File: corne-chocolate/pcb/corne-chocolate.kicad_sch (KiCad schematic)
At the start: 19 parts, among them J2 nice!view, J3 Battery, J4 Battery, SW21 1.5U, SW22 SW_PUSH, SW23 SW_SPDT, U1 ProMicro

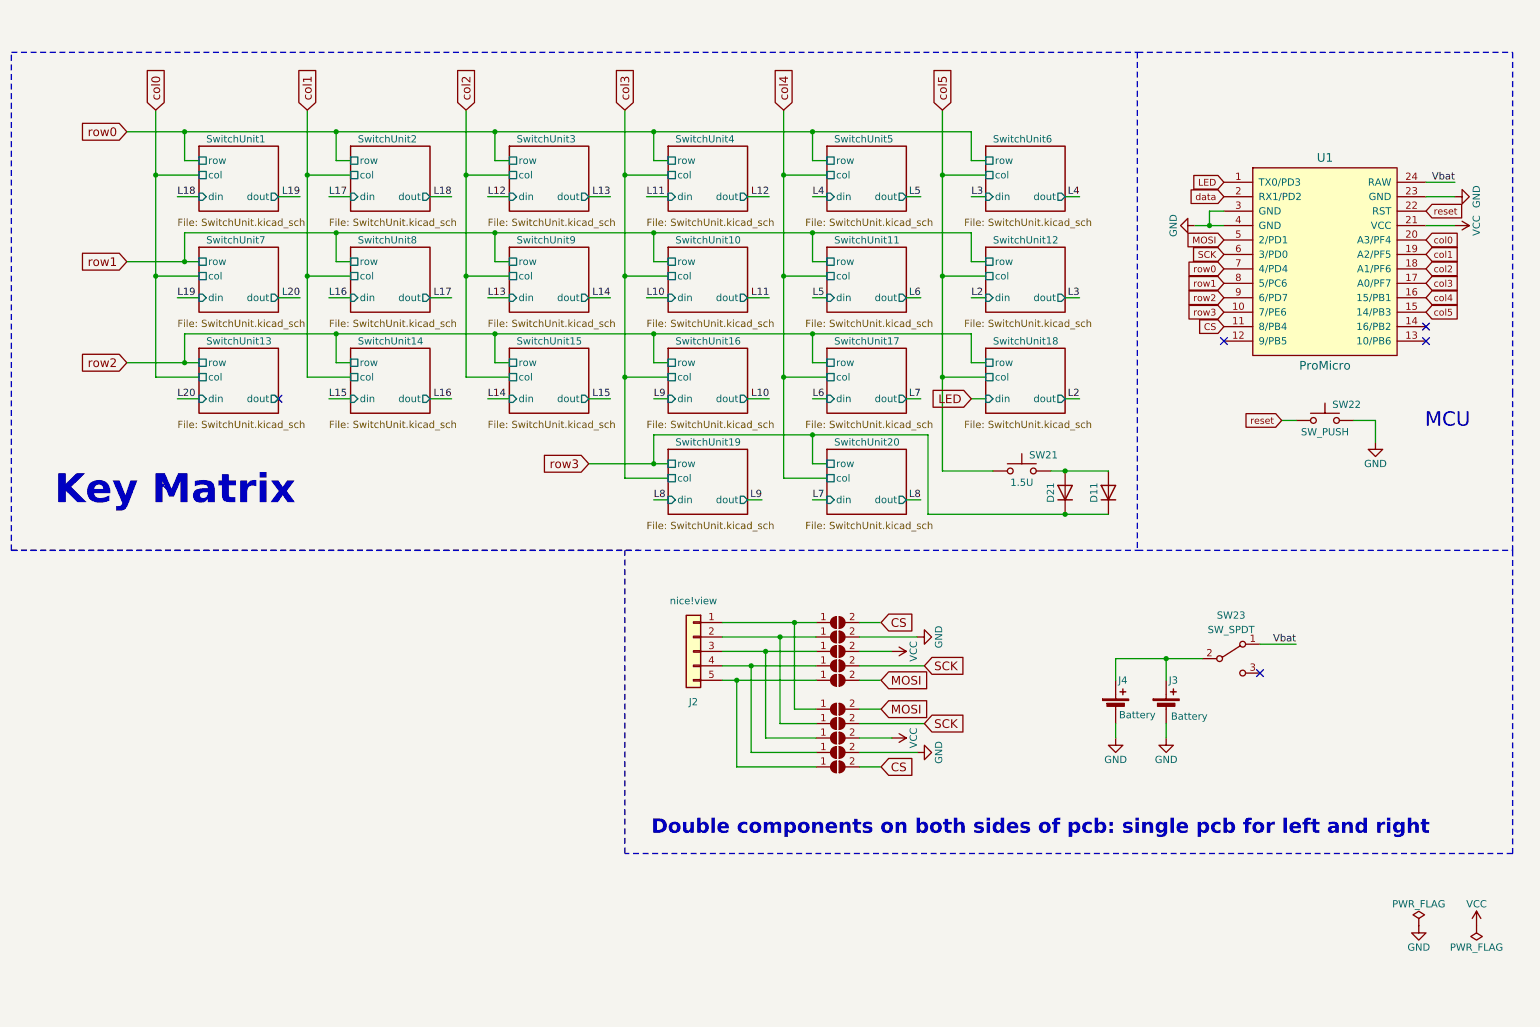
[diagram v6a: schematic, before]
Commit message: pcb remove per-switch LEDs
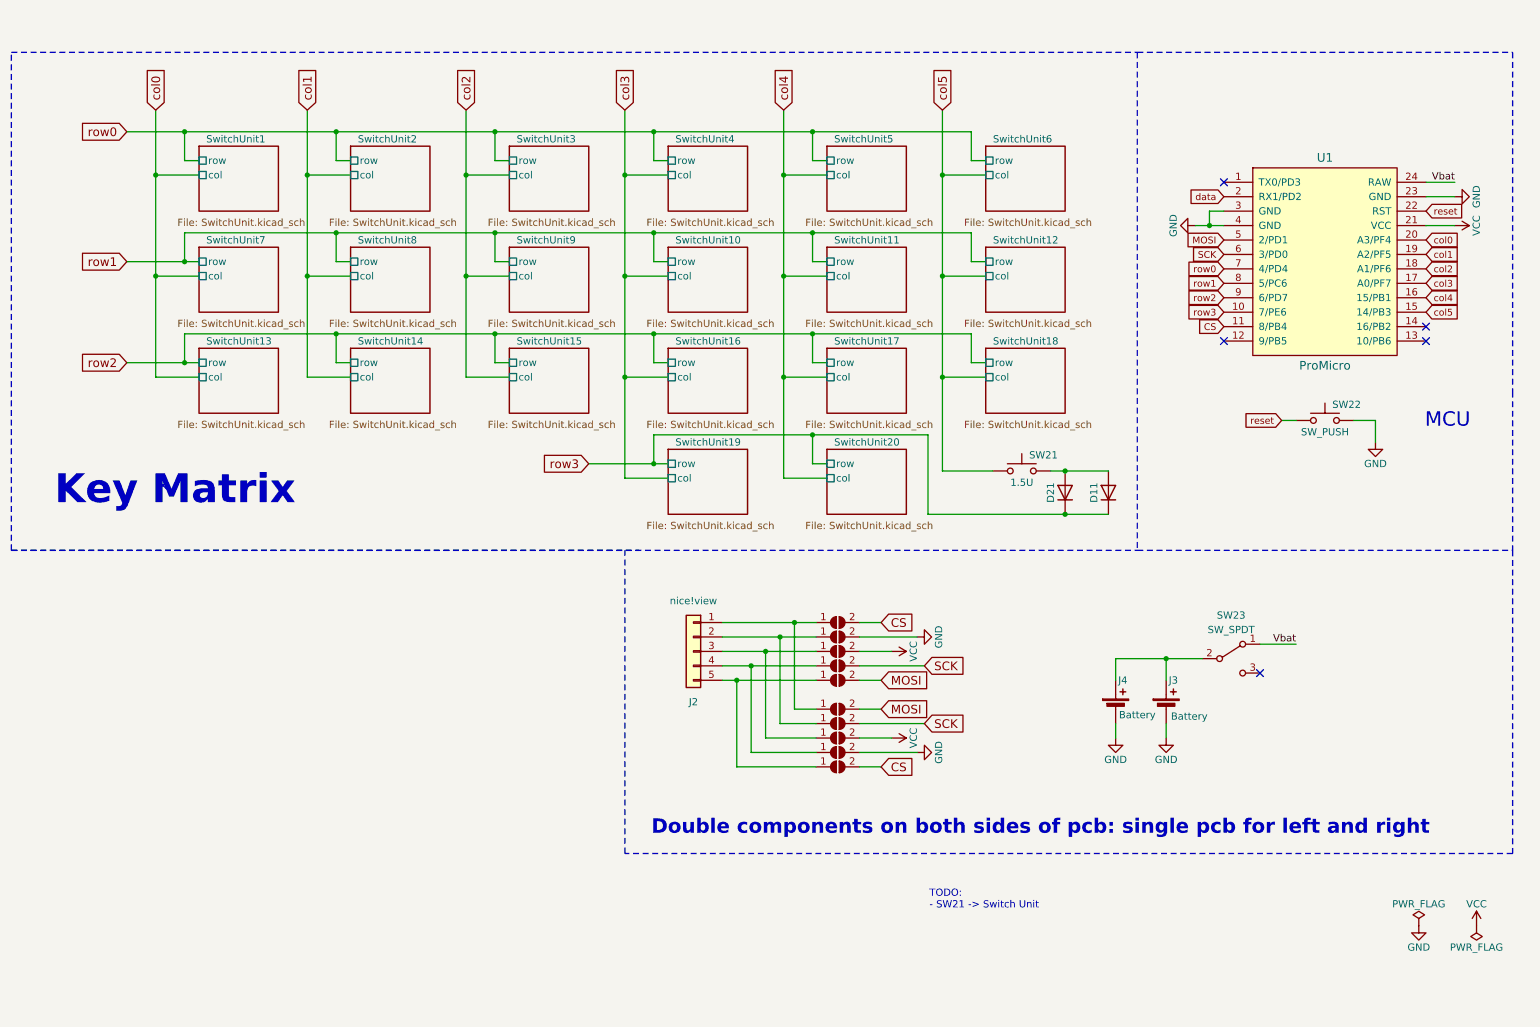
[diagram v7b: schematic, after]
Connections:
- net LED: no longer names the net of U1.1 (TX0/PD3)
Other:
- sheet SwitchUnit1 ports: added none; removed din, dout
- sheet SwitchUnit10 ports: added none; removed din, dout
- sheet SwitchUnit11 ports: added none; removed din, dout
- sheet SwitchUnit12 ports: added none; removed din, dout
- sheet SwitchUnit13 ports: added none; removed din, dout
- sheet SwitchUnit14 ports: added none; removed din, dout
- sheet SwitchUnit15 ports: added none; removed din, dout
- sheet SwitchUnit16 ports: added none; removed din, dout
- sheet SwitchUnit17 ports: added none; removed din, dout
- sheet SwitchUnit18 ports: added none; removed din, dout
- sheet SwitchUnit19 ports: added none; removed din, dout
- sheet SwitchUnit2 ports: added none; removed din, dout
- sheet SwitchUnit20 ports: added none; removed din, dout
- sheet SwitchUnit3 ports: added none; removed din, dout
- sheet SwitchUnit4 ports: added none; removed din, dout
- sheet SwitchUnit5 ports: added none; removed din, dout
- sheet SwitchUnit6 ports: added none; removed din, dout
- sheet SwitchUnit7 ports: added none; removed din, dout
- sheet SwitchUnit8 ports: added none; removed din, dout
- sheet SwitchUnit9 ports: added none; removed din, dout
- note added: "TODO: - SW21 -> Switch Unit"

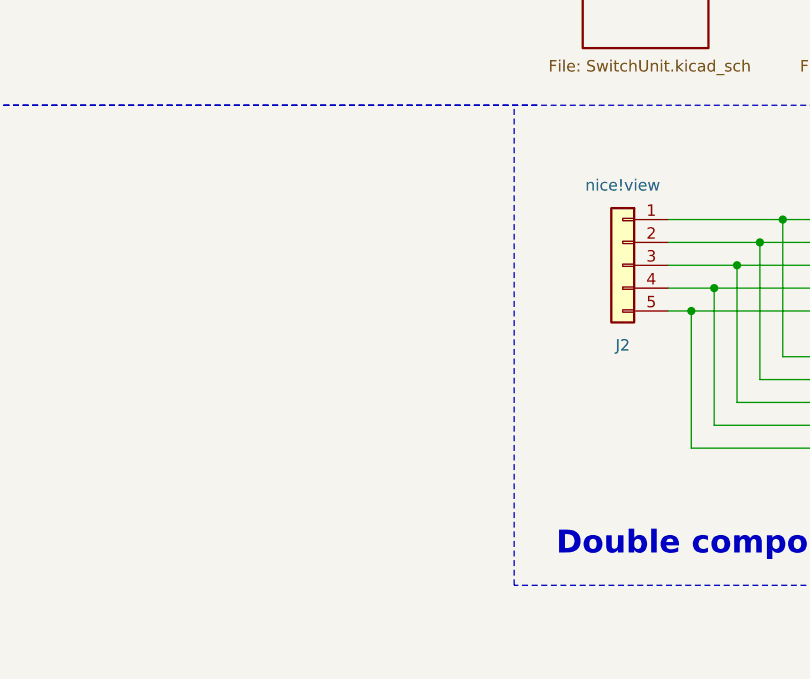
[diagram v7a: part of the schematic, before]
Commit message: pcb clean up mounting holes
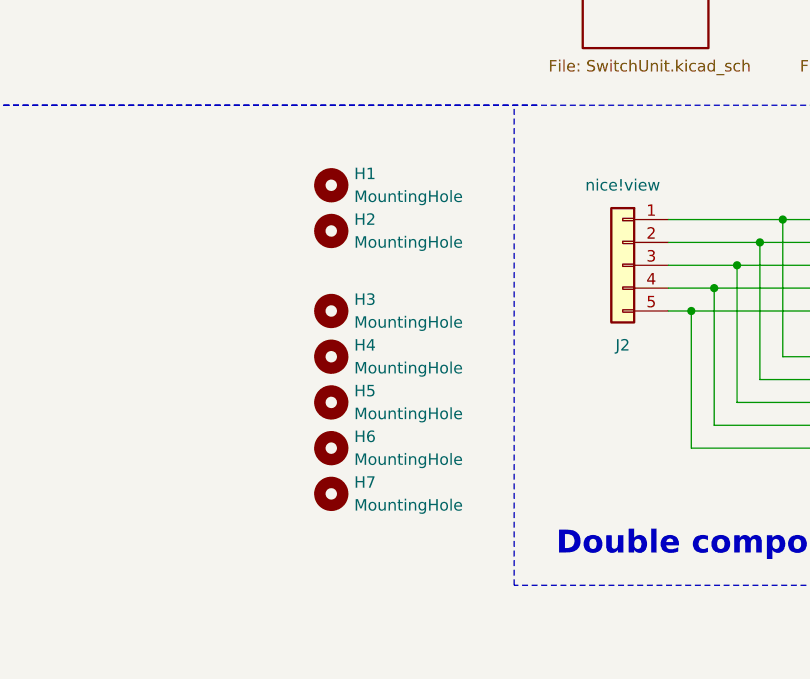
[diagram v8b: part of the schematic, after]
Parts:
- added H1, H2: MountingHole, MountingHole:MountingHole_2.2mm_M2, symbol Mechanical:MountingHole
- added H3, H4, H5, H6, H7: MountingHole, MountingHole:MountingHole_4.3mm_M4, symbol Mechanical:MountingHole
